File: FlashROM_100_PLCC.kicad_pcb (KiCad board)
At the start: 2 copper layers, 16.5 x 34.3 mm, 7 parts, among them J1 LH535618 DIP LEGS, U1 29F010

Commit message: kicad 6
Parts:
- JP1: value ~CS~ breakout -> ~{CS} breakout
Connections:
- net /ALE_~WE renamed /ALE_~{WE}
- net /~CS renamed /~{CS}
- net /~CS_BUS renamed /~{CS_BUS}
- net /~OE renamed /~{OE}
- net /~WE renamed /~{WE}
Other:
- net class Default removed
- board text added: "Connect ~{CS} OUT to REX TP1. Leave ~{CS} IN unconnected."
- board text added: "If REX is later removed, connect ~{CS} OUT to ~{CS} IN."
- board text added: "Install a shunt on ~{CS}, or, install wires as above,"
- board text added: "Run 2 wires from ~{CS} IN & ~{CS} OUT to Option ROM compartment."
- board text added: "~{CS}"
- board text removed: "Connect ~CS~ OUT to REX TP1. Leave ~CS~ IN unconnected."
- board text removed: "If REX is later removed, connect ~CS~ OUT to ~CS~ IN."
- board text removed: "Install a shunt on ~CS~, or, install wires as above,"
- board text removed: "Run 2 wires from ~CS~ IN & ~CS~ OUT to Option ROM compartment."
- board text removed: "~CS"

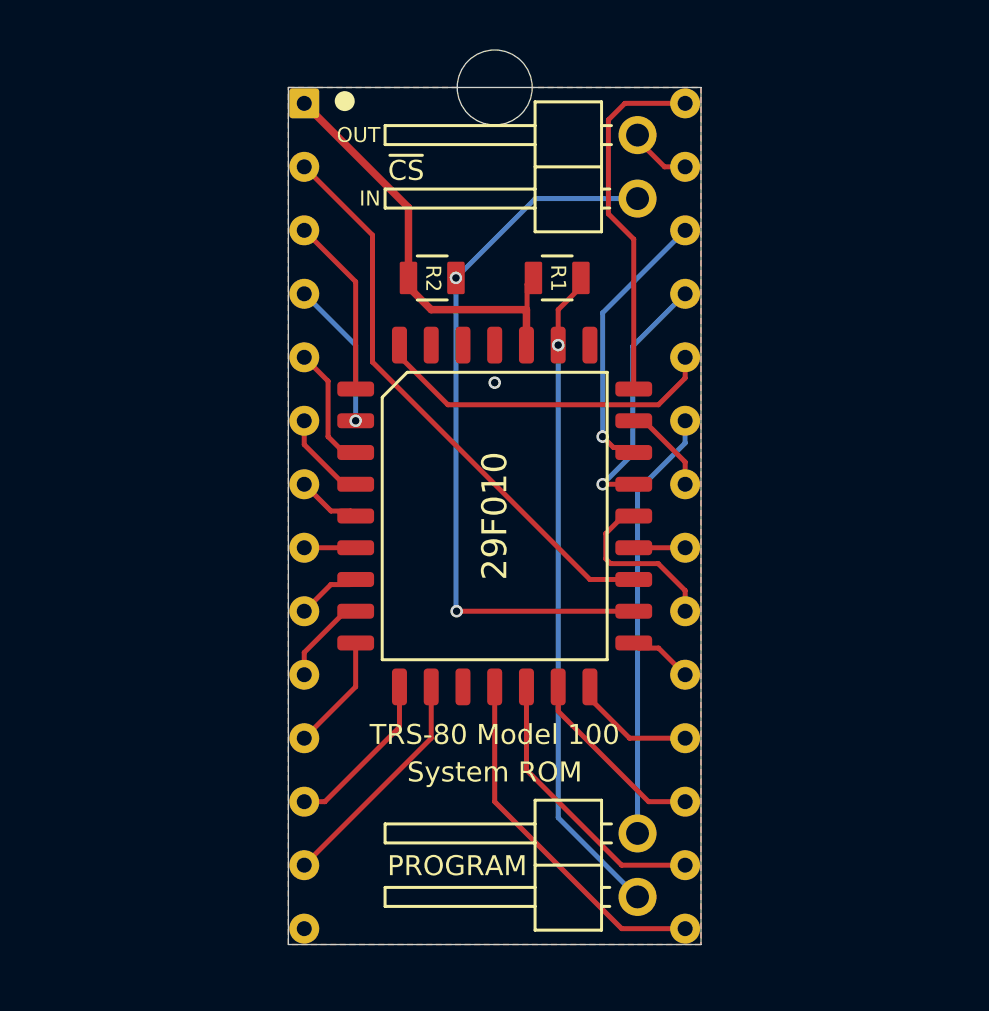
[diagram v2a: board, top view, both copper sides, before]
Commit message: flashrom_100_plcc outline
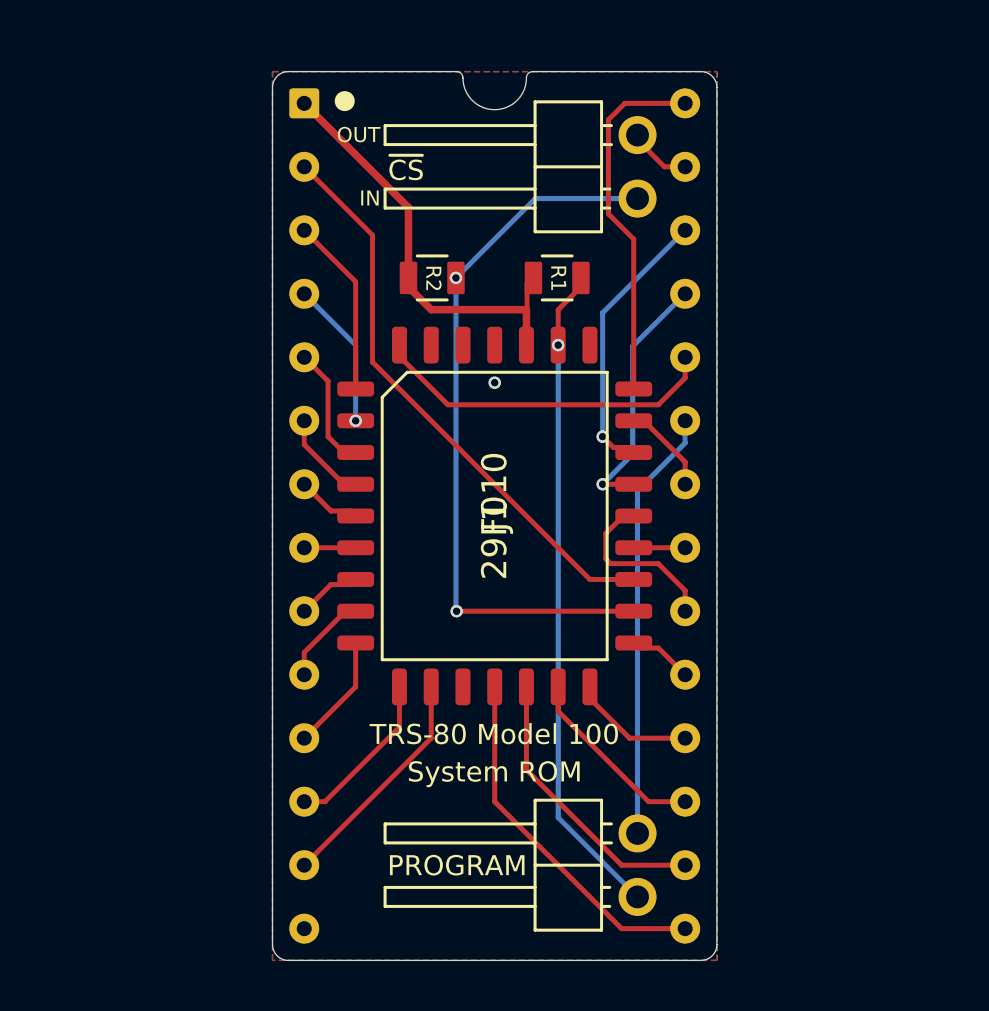
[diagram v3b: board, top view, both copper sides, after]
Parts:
- removed REF**: NPTH_3mm, 000_LOCAL:NPTH_3mm
- J1: footprint 000_LOCAL:DIP28_0.6_pcb_sil_pins -> 000_LOCAL:DIP28_0.6_pcb
- JP1: value ~{CS} breakout -> ~CS~ breakout
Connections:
- U1 pad 1: (no net) -> unconnected-(U1-Pad1)
- U1 pad 30: (no net) -> unconnected-(U1-Pad30)
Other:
- board size 16.5 x 34.3 mm -> 17.8 x 35.6 mm

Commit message: various minor cleanups
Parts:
- JP1: value ~CS~ breakout -> ~{CS} breakout
- moved JP2 23.0 mm to (165.2, 94.3), turned to -90 degrees
- moved JP1 19.7 mm to (137.3, 94.3), turned to -90 degrees
- moved R1 13.9 mm to (140.5, 97.5), turned to -90 degrees
- moved R2 13.9 mm to (140.5, 102.5), turned to -90 degrees
- turned J1 to 90 degrees
- turned U1 to 90 degrees
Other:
- board size 17.8 x 35.6 mm -> 35.6 x 17.8 mm
- board text added: "${COMMENT2} ${TITLE} ${REVISION}"
- board text added: "R1,R2: ${00000000-0000-0000-0000-0000604ac043:VALUE} Legs: TE 1544210"
- board text added: "REX_Classic main ROM support: ~{CS}_OUT to REX TP1 to boot from REX main rom ~{CS}_OUT to ~{CS}_IN to boot from internal main rom"
- board text removed: "Connect ~{CS} OUT to REX TP1. Leave ~{CS} IN unconnected."
- board text removed: "If REX is later removed, connect ~{CS} OUT to ~{CS} IN."
- board text removed: "Install a shunt on ~{CS}, or, install wires as above,"
- board text removed: "Legs: TE 1544210"
- board text removed: "R1, R2: 47k"
- board text removed: "REX can then be added later without disassembling."
- board text removed: "Run 2 wires from ~{CS} IN & ~{CS} OUT to Option ROM compartment."
- board text removed: "To use REX Main ROM feature:"
- board text removed: "To use without REX:"
- board text removed: "and connect them to each other in the Option ROM compartment."

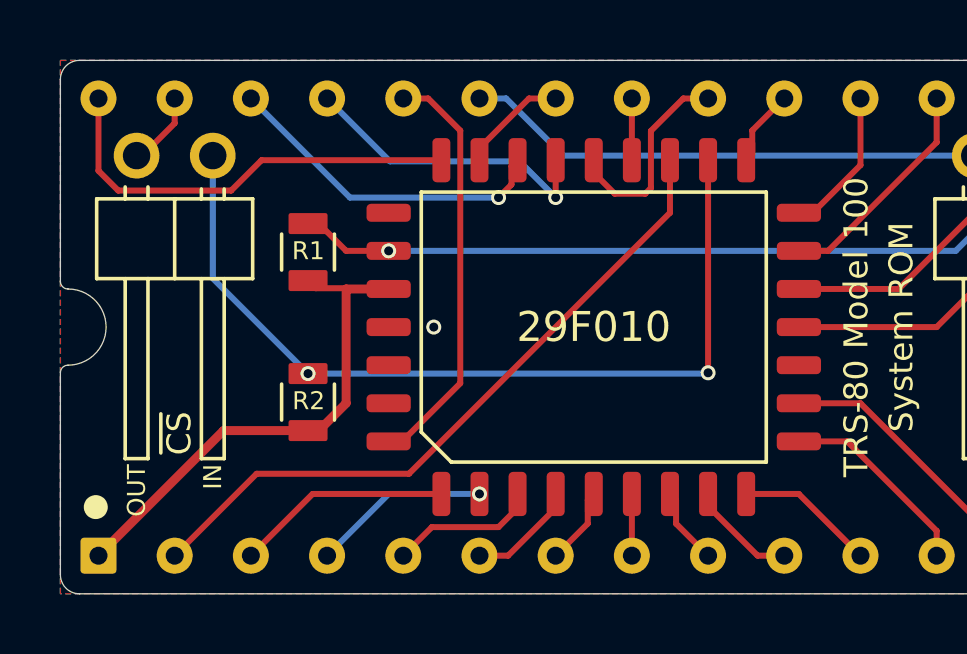
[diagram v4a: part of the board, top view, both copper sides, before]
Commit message: flashrom_100 pin names & minor trace move
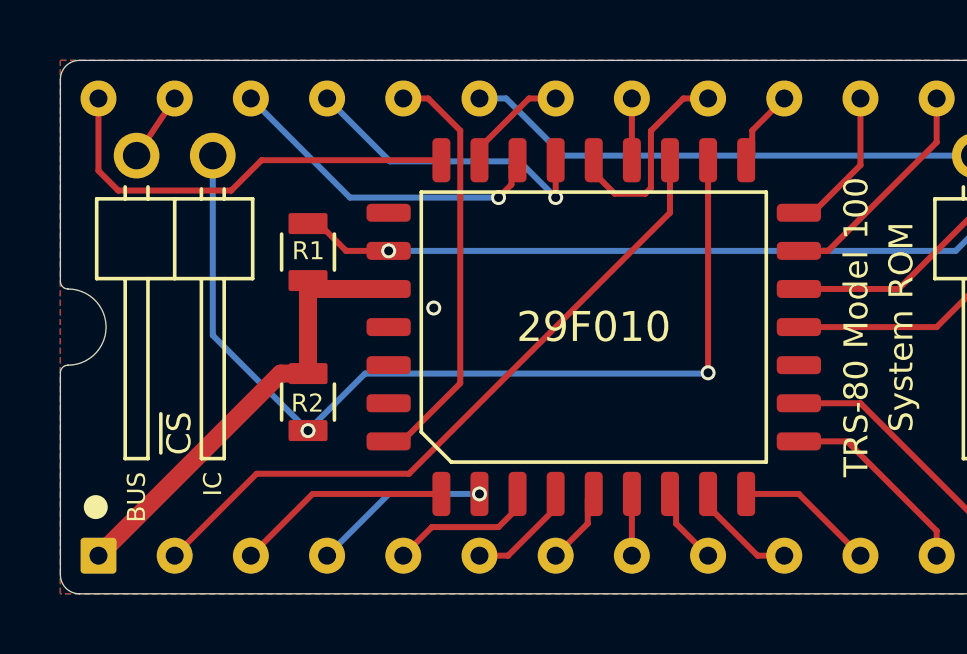
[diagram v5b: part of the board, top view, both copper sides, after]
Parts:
- R1, R2: value 47K -> 100K
- turned R2 to 90 degrees
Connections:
- net /~{CS} renamed /~{CS_IC}
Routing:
- net /~{CS_IC}: track 29.0 -> 31.7 mm
- net VCC: track 17.2 -> 15.7 mm
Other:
- board text added: "BUS"
- board text added: "IC"
- board text added: "REX_Classic main ROM support: ~{CS_BUS} to REX TP1 to boot from REX main rom ~{CS_BUS} to ~{CS_IC} to boot from internal main rom"
- board text removed: "IN"
- board text removed: "OUT"
- board text removed: "REX_Classic main ROM support: ~{CS}_OUT to REX TP1 to boot from REX main rom ~{CS}_OUT to ~{CS}_IN to boot from internal main rom"
